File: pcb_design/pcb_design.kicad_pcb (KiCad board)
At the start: 2 copper layers, 81.9 x 74.9 mm, 42 parts, among them J1 PWR_IN, J10 PD, J11 PE, J12 PF, J13 ICSP, J14 PWR_OUT, J15 Conn_01x04, J2 ESP8266_CONN, J3 PL, J4 PK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

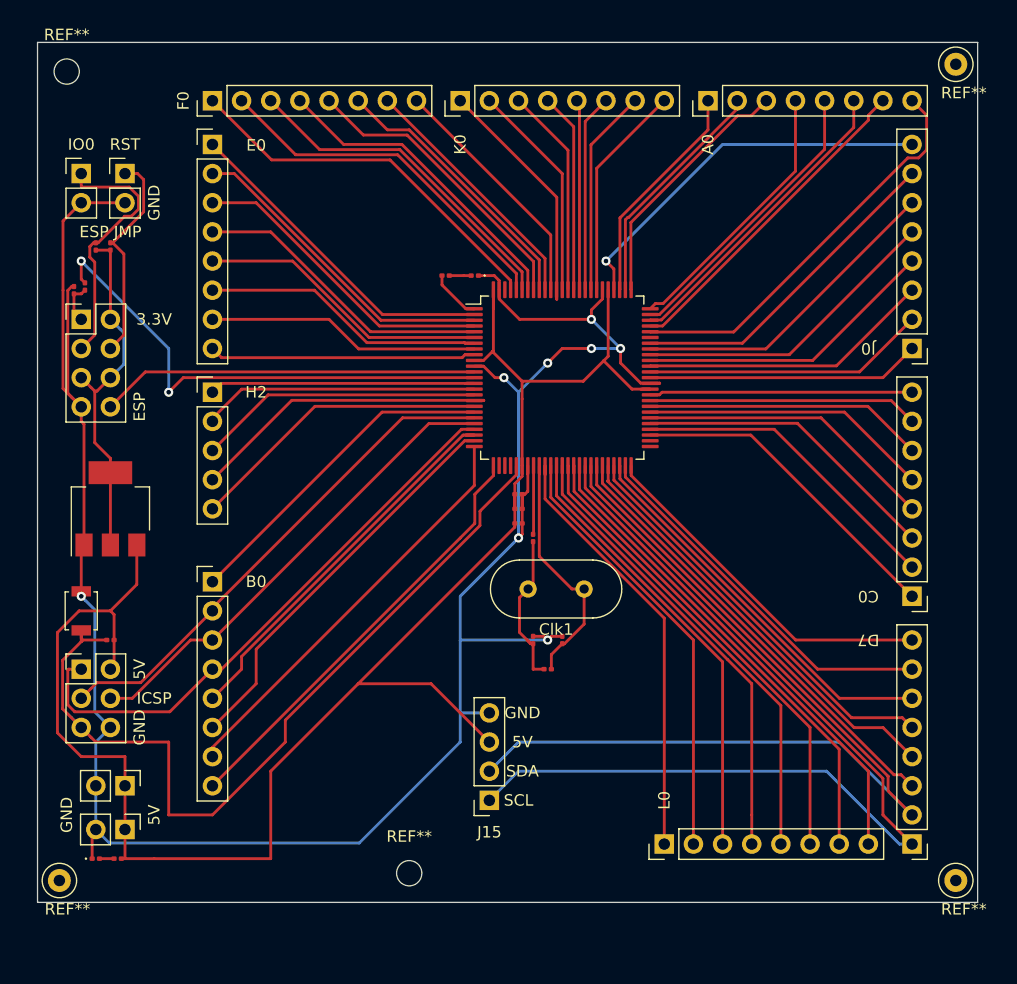
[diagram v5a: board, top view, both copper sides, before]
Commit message: 0603EU -> 0603US
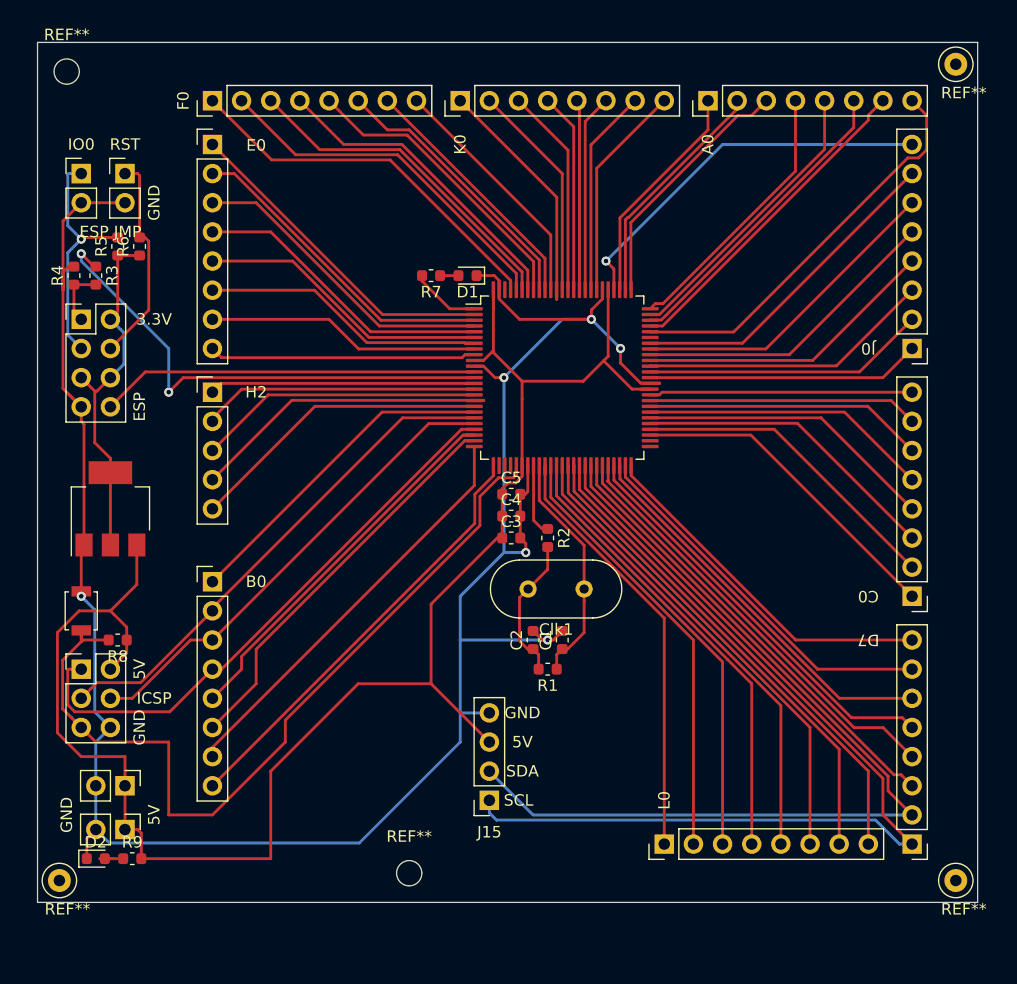
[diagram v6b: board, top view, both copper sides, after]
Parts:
- C1, C2, C3, C4, C5: footprint Capacitor_SMD:C_0201_0603Metric -> Capacitor_SMD:C_0603_1608Metric
- D1, D2: footprint LED_SMD:LED_0201_0603Metric -> LED_SMD:LED_0603_1608Metric
- R1, R2, R3, R4, R5, R6, R7, R8, R9: footprint Resistor_SMD:R_0201_0603Metric -> Resistor_SMD:R_0603_1608Metric
- moved R6 2.54 mm to (104.1, 52.1)
- moved R5 1.91 mm to (102.2, 52.1)
- moved C3 1.42 mm to (136.5, 77.5)
- moved R3 1.34 mm to (100.3, 54.6)
- moved R7 1.27 mm to (129.5, 54.6)
- moved R4 1.27 mm to (98.4, 54.6)
- moved R9 1.27 mm to (103.5, 105.4)
- moved R2 1.27 mm to (139.7, 77.5)
- moved C4 0.90 mm to (136.5, 75.6)
- moved R8 0.64 mm to (102.2, 86.4)
- moved C5 0.63 mm to (136.5, 73.7)
- moved D1 0.63 mm to (132.7, 54.6)
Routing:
- net GND: track 205.4 -> 201.0 mm, vias 11 -> 9
- net +5V: track 153.1 -> 150.7 mm
- net /SDA: track 82.3 -> 80.2 mm
- net /ESP_IO0: track 22.7 -> 21.1 mm, vias 0 -> 3
- net /ESP_RX: track 3.57 -> 5.19 mm
- net Net-(D2-Pad2): track 1.27 -> 2.86 mm
- net Net-(R7-Pad2): track 4.62 -> 6.16 mm
- net /SCL: track 85.1 -> 83.6 mm
- net /RST: track 74.3 -> 75.2 mm
- net Net-(C1-Pad1): track 21.5 -> 20.6 mm
